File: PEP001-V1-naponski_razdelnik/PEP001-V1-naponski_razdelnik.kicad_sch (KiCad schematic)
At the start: 11 parts, among them J1 Screw_Terminal_01x02

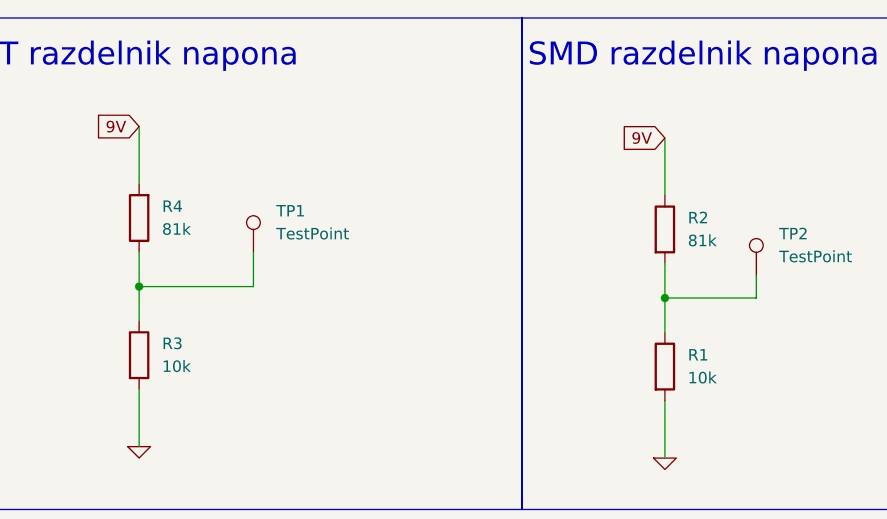
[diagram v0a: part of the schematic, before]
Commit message: PEP001-V1_BOM_CPL
-Added JLC component numbers
-Generated BOM csv file for SMD components
-Generated CPL csv file for SMD components
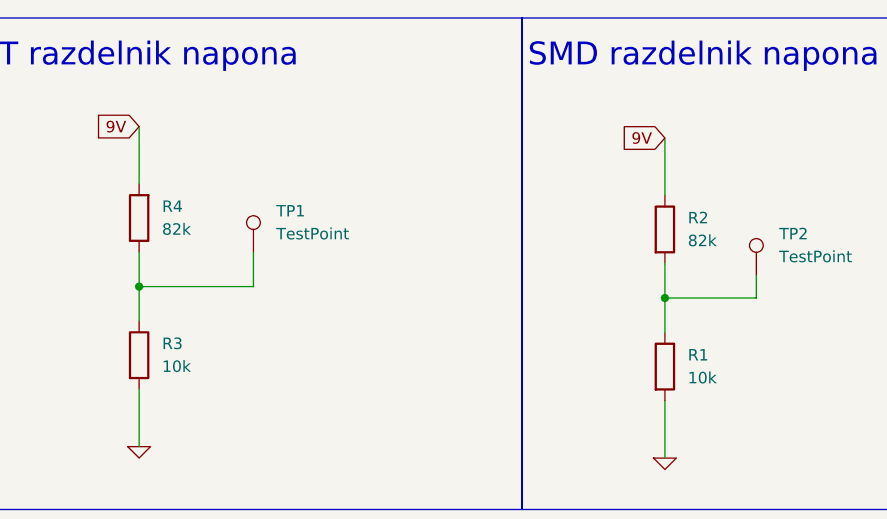
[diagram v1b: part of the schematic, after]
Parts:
- J1: JLCPCB Footprint (none) -> THT; LCSC (none) -> C3018698
- R1: JLCPCB Footprint (none) -> 1206; LCSC (none) -> C17902; now left out of the parts list
- R2: value 81k -> 82k; JLCPCB Footprint (none) -> 1206; LCSC (none) -> C17979
- R3: JLCPCB Footprint (none) -> THT; LCSC (none) -> C410695
- R4: value 81k -> 82k; JLCPCB Footprint (none) -> THT; LCSC (none) -> C601724
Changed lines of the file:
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@@
 (kicad_sch
-	(version 20231120)
+	(version 20250114)
 	(generator "eeschema")
-	(generator_version "8.0")
+	(generator_version "9.0")
 	(paper "A5")
 	(title_block
@@
 		(rev "v1")
 	)
+	(rectangle
+		(start 12.065 12.065)
+		(end 69.85 66.675)
+		(stroke
+			(width 0)
+			(type default)
+		)
+		(fill
+			(type none)
+		)
+	)
+	(rectangle
+		(start 12.065 104.14)
+		(end 83.82 135.89)
+		(stroke
+			(width 0)
+			(type default)
+		)
+		(fill
+			(type none)
+		)
+	)
+	(rectangle
+		(start 69.85 12.065)
+		(end 133.985 66.675)
+		(stroke
+			(width 0)
+			(type default)
+		)
+		(fill
+			(type none)
+		)
+	)
+	(rectangle
+		(start 133.985 12.065)
+		(end 198.12 66.675)
+		(stroke
+			(width 0)
+			(type default)
+		)
+		(fill
+			(type none)
+		)
+	)
+	(text "SMD razdelnik napona\n"
+		(exclude_from_sim no)
+		(at 134.62 17.78 0)
+		(effects
+			(font
+				(size 2.54 2.54)
+			)
+			(justify left bottom)
+		)
+	)
+	(text "Rupe za montiranje\n"
+		(exclude_from_sim no)
+		(at 17.78 109.22 0)
+		(effects
+			(font
+				(size 2.54 2.54)
+			)
+			(justify left bottom)
+		)
+	)
+	(text "Konektor za napajanje"
+		(exclude_from_sim no)
+		(at 12.7 17.78 0)
+		(effects
+			(font
+				(size 2.54 2.54)
+			)
+			(justify left bottom)
+		)
+	)
+	(text "THT razdelnik napona\n"
+		(exclude_from_sim no)
+		(at 71.12 17.78 0)
+		(effects
+			(font
+				(size 2.54 2.54)
+			)
+			(justify left bottom)
+		)
+	)
 	(junction
 		(at 149.86 43.18)
@@
 			(width 0)
 			(type default)
-		)
-	)
-	(rectangle
-		(start 12.065 12.065)
-		(end 69.85 66.675)
-		(stroke
-			(width 0)
-			(type default)
-		)
-		(fill
-			(type none)
-		)
-	)
-	(rectangle
-		(start 12.065 104.14)
-		(end 83.82 135.89)
-		(stroke
-			(width 0)
-			(type default)
-		)
-		(fill
-			(type none)
-		)
-	)
-	(rectangle
-		(start 69.85 12.065)
-		(end 133.985 66.675)
-		(stroke
-			(width 0)
-			(type default)
-		)
-		(fill
-			(type none)
-		)
-	)
-	(rectangle
-		(start 133.985 12.065)
-		(end 198.12 66.675)
-		(stroke
-			(width 0)
-			(type default)
-		)
-		(fill
-			(type none)
-		)
-	)
-	(text "SMD razdelnik napona\n"
-		(exclude_from_sim no)
-		(at 134.62 17.78 0)
-		(effects
-			(font
-				(size 2.54 2.54)
-			)
-			(justify left bottom)
-		)
-	)
-	(text "Rupe za montiranje\n"
-		(exclude_from_sim no)
-		(at 17.78 109.22 0)
-		(effects
-			(font
-				(size 2.54 2.54)
-			)
-			(justify left bottom)
-		)
-	)
-	(text "Konektor za napajanje"
-		(exclude_from_sim no)
-		(at 12.7 17.78 0)
-		(effects
-			(font
-				(size 2.54 2.54)
-			)
-			(justify left bottom)
-		)
-	)
-	(text "THT razdelnik napona\n"
-		(exclude_from_sim no)
-		(at 71.12 17.78 0)
-		(effects
-			(font
-				(size 2.54 2.54)
-			)
-			(justify left bottom)
 		)
 	)
@@
 			)
 		)
-		(property "Value" "81k"
+		(property "Value" "82k"
 			(at 152.4 36.8299 0)
 			(effects
@@
 			)
 		)
-		(property "Datasheet" "~"
+		(property "Datasheet" "https://www.lcsc.com/datasheet/lcsc_datasheet_2206010145_UNI-ROYAL-Uniroyal-Elec-1206W4F8202T5E_C17979.pdf"
 			(at 149.86 35.56 0)
 			(effects
@@
 		)
 		(property "Description" ""
+			(at 149.86 35.56 0)
+			(effects
+				(font
+					(size 1.27 1.27)
+				)
+				(hide yes)
+			)
+		)
+		(property "LCSC" "C17979"
+			(at 149.86 35.56 0)
+			(effects
+				(font
+					(size 1.27 1.27)
+				)
+				(hide yes)
+			)
+		)
+		(property "JLCPCB Footprint" "1206"
 			(at 149.86 35.56 0)
 			(effects
@@
 			)
 		)
-		(property "Datasheet" "~"
+		(property "Datasheet" "https://www.lcsc.com/datasheet/lcsc_datasheet_2304140030_TyoHM-RN1-4W10KFT-BA1_C410695.pdf"
 			(at 91.44 49.53 0)
 			(effects
@@
 		)
 		(property "Description" ""
+			(at 91.44 49.53 0)
+			(effects
+				(font
+					(size 1.27 1.27)
+				)
+				(hide yes)
+			)
+		)
+		(property "LCSC" "C410695"
+			(at 91.44 49.53 0)
+			(effects
+				(font
+					(size 1.27 1.27)
+				)
+				(hide yes)
+			)
+		)
+		(property "JLCPCB Footprint" "THT"
 			(at 91.44 49.53 0)
 			(effects
@@
 		(at 40.64 38.1 0)
 		(unit 1)
-		(exclude_from_sim yes)
+		(exclude_from_sim no)
 		(in_bom yes)
 		(on_board yes)
@@
 			)
 		)
-		(property "Datasheet" "~"
+		(property "Datasheet" "https://wmsc.lcsc.com/wmsc/upload/file/pdf/v2/lcsc/2301061230_DORABO-DB127V-5-08-2P-GN-S_C3018698.pdf"
 			(at 40.64 38.1 0)
 			(effects
@@
 		)
 		(property "Description" ""
+			(at 40.64 38.1 0)
+			(effects
+				(font
+					(size 1.27 1.27)
+				)
+				(hide yes)
+			)
+		)
+		(property "LCSC" "C3018698"
+			(at 40.64 38.1 0)
+			(effects
+				(font
+					(size 1.27 1.27)
+				)
+				(hide yes)
+			)
+		)
+		(property "JLCPCB Footprint" "THT"
 			(at 40.64 38.1 0)
 			(effects
@@
 		(unit 1)
 		(exclude_from_sim no)
-		(in_bom yes)
+		(in_bom no)
 		(on_board yes)
 		(dnp no)
@@
 			)
 		)
-		(property "Datasheet" "~"
+		(property "Datasheet" "https://jlcpcb.com/api/file/downloadByFileSystemAccessId/8579705876598476800"
 			(at 149.86 50.8 0)
 			(effects
@@
 		)
 		(property "Description" ""
+			(at 149.86 50.8 0)
+			(effects
+				(font
+					(size 1.27 1.27)
+				)
+				(hide yes)
+			)
+		)
+		(property "LCSC" "C17902"
+			(at 149.86 50.8 0)
+			(effects
+				(font
+					(size 1.27 1.27)
+				)
+				(hide yes)
+			)
+		)
+		(property "JLCPCB Footprint" "1206"
 			(at 149.86 50.8 0)
 			(effects
@@
 			)
 		)
-		(property "Value" "81k"
+		(property "Value" "82k"
 			(at 93.98 35.5599 0)
 			(effects
@@
 			)
 		)
-		(property "Datasheet" "~"
+		(property "Datasheet" "https://wmsc.lcsc.com/wmsc/upload/file/pdf/v2/lcsc/2304140030_VO-MF1-4W-82K-1--OT26_C601724.pdf"
 			(at 91.44 34.29 0)
 			(effects
@@
 		)
 		(property "Description" ""
+			(at 91.44 34.29 0)
+			(effects
+				(font
+					(size 1.27 1.27)
+				)
+				(hide yes)
+			)
+		)
+		(property "LCSC" "C601724"
+			(at 91.44 34.29 0)
+			(effects
+				(font
+					(size 1.27 1.27)
+				)
+				(hide yes)
+			)
+		)
+		(property "JLCPCB Footprint" "THT"
 			(at 91.44 34.29 0)
 			(effects
@@
 		)
 	)
+	(embedded_fonts no)
 )

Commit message: Component info
Generated csv file with all component datasheets and LCSC part numbers for future reference
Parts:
- R1: now in the parts list
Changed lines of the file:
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@@
 		(unit 1)
 		(exclude_from_sim no)
-		(in_bom no)
+		(in_bom yes)
 		(on_board yes)
 		(dnp no)
